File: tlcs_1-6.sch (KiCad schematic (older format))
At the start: 66 parts, among them U3 TLC5941, U4 TLC5941, U5 TLC5941, U6 TLC5941, U7 TLC5941, U8 TLC5941

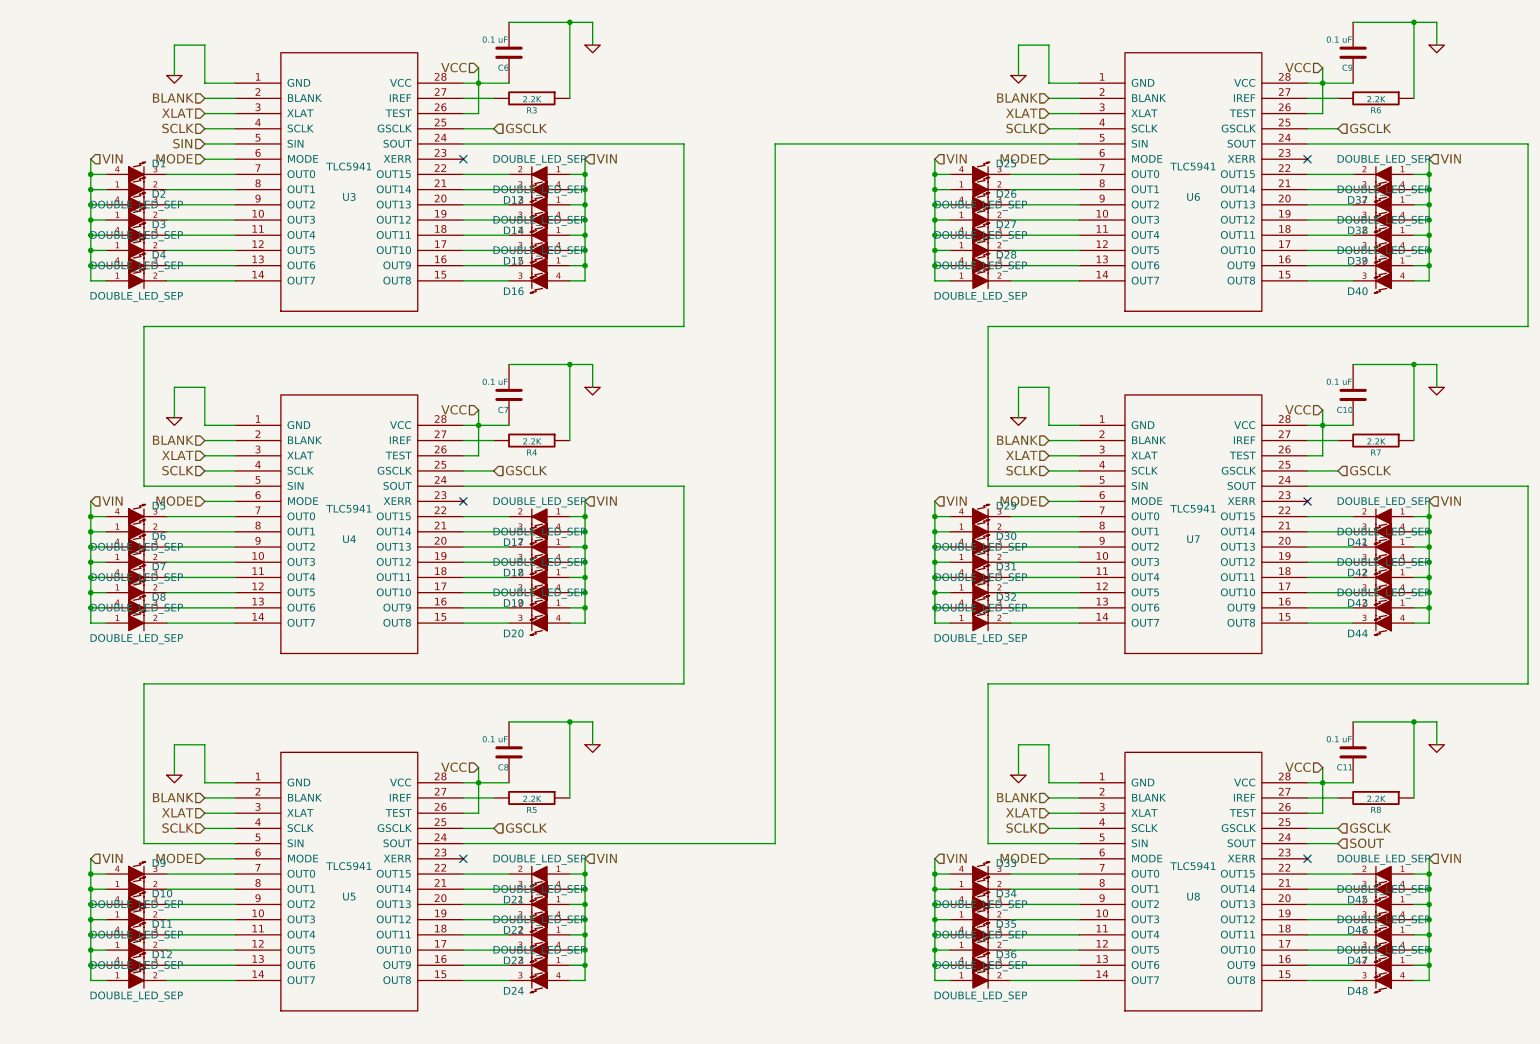
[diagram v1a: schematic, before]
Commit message: partially changed LEDs
done new footprint, added to new tca_footprints.pretty library. partially changed LEDs in schematic.
committing to go back and double check previous LED order to maintain firmware compatibility.
added /rescue-backup/ to git ignore (dont need with version control)
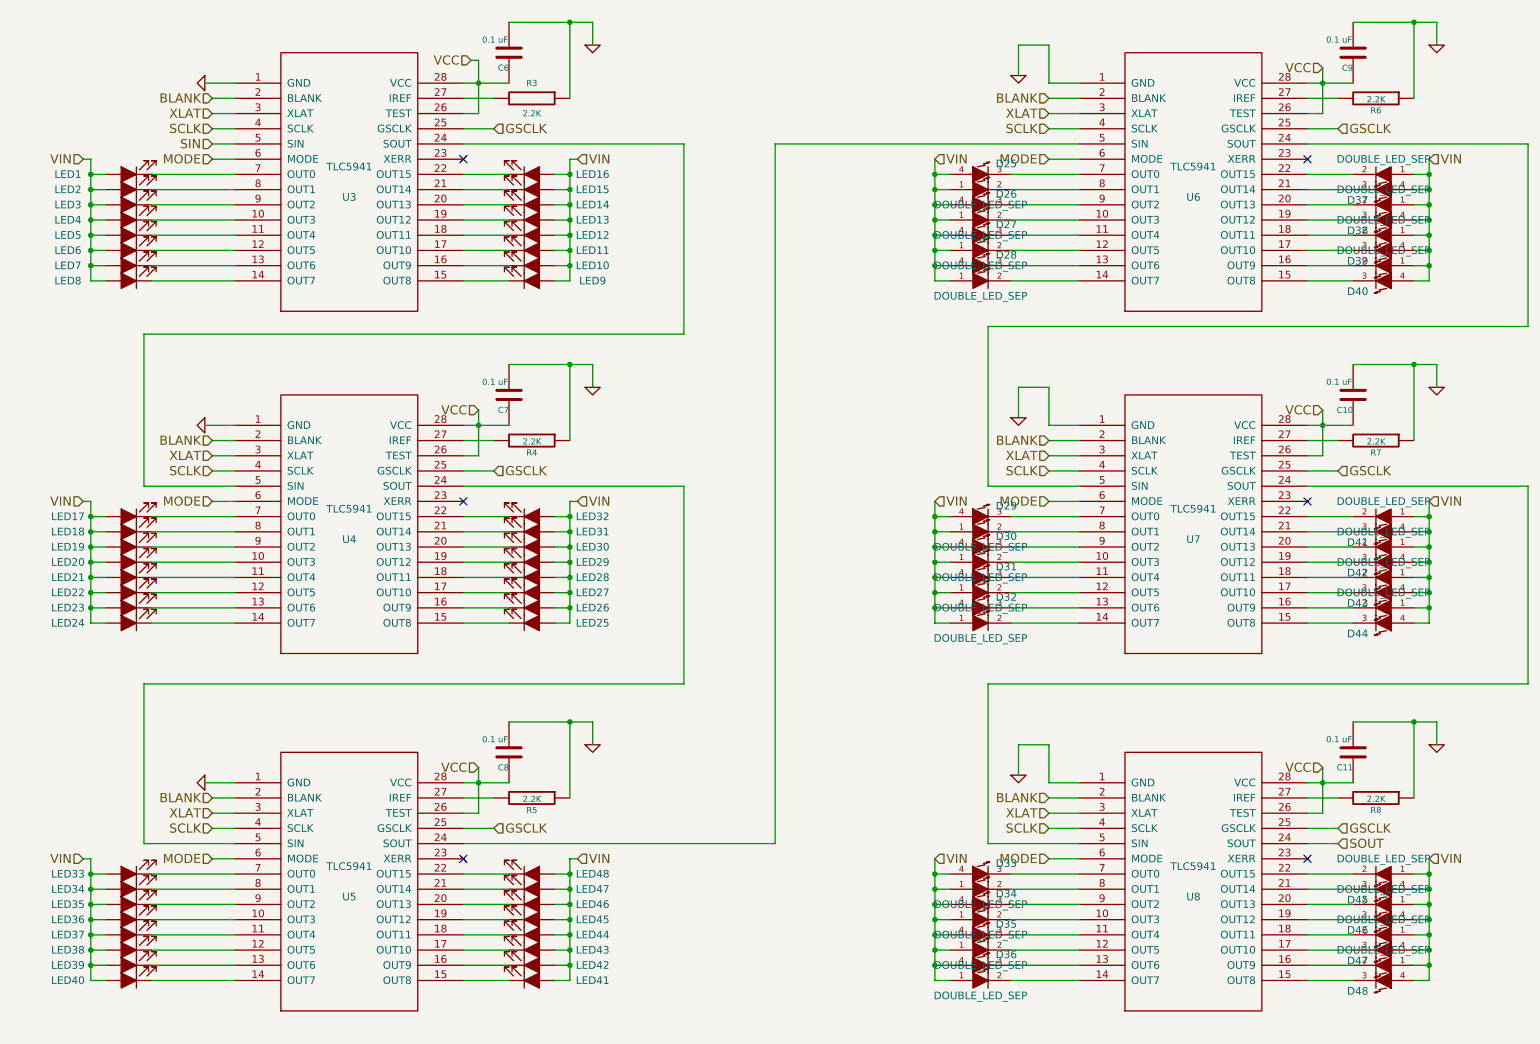
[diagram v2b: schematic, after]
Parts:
- removed D1, D10, D11, D12, D13, D14, D15, D16, D17, D18, D19, D2, D20, D21, D22, D23, D24, D3, D4, D5, D6, D7, D8, D9: DOUBLE_LED_SEP, SMD_0805_4PIN, symbol tca-rescue:DOUBLE_LED_SEP
- added LED1, LED10, LED11, LED12, LED13, LED14, LED15, LED16, LED17, LED18, LED19, LED2, LED20, LED21, LED22, LED23, LED24, LED25, LED26, LED27, LED28, LED29, LED3, LED30, LED31, LED32, LED33, LED34, LED35, LED36, LED37, LED38, LED39, LED4, LED40, LED41, LED42, LED43, LED44, LED45, LED46, LED47, LED48, LED5, LED6, LED7, LED8, LED9: LED_ALT, tca_footprints:VLDx1232G, symbol Device:LED_ALT
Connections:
- net VIN: now also LED1.2 (A), LED10.2 (A), LED11.2 (A), LED12.2 (A), LED13.2 (A), LED14.2 (A), LED15.2 (A), LED16.2 (A), LED17.2 (A), LED18.2 (A), LED19.2 (A), LED2.2 (A), LED20.2 (A), LED21.2 (A), LED22.2 (A), LED23.2 (A), LED24.2 (A), LED25.2 (A), LED26.2 (A), LED27.2 (A), LED28.2 (A), LED29.2 (A), LED3.2 (A), LED30.2 (A), LED31.2 (A), LED32.2 (A), LED33.2 (A), LED34.2 (A), LED35.2 (A), LED36.2 (A), LED37.2 (A), LED38.2 (A), LED39.2 (A), LED4.2 (A), LED40.2 (A), LED41.2 (A), LED42.2 (A), LED43.2 (A), LED44.2 (A), LED45.2 (A), LED46.2 (A), LED47.2 (A), LED48.2 (A), LED5.2 (A), LED6.2 (A), LED7.2 (A), LED8.2 (A), LED9.2 (A)
- net at U4.10 (OUT3): now also LED20.1 (K)
- net at U4.11 (OUT4): now also LED21.1 (K)
- net at U4.12 (OUT5): now also LED22.1 (K)
- net at U4.13 (OUT6): now also LED23.1 (K)
- net at U4.14 (OUT7): now also LED24.1 (K)
- net at U4.15 (OUT8): now also LED25.1 (K)
- net at U4.16 (OUT9): now also LED26.1 (K)
- net at U4.17 (OUT10): now also LED27.1 (K)
- net at U4.18 (OUT11): now also LED28.1 (K)
- net at U4.19 (OUT12): now also LED29.1 (K)
- net at U4.20 (OUT13): now also LED30.1 (K)
- net at U4.21 (OUT14): now also LED31.1 (K)
- net at U4.22 (OUT15): now also LED32.1 (K)
- net at U4.7 (OUT0): now also LED17.1 (K)
- net at U4.8 (OUT1): now also LED18.1 (K)
- net at U4.9 (OUT2): now also LED19.1 (K)
- net at U3.10 (OUT3): now also LED4.1 (K)
- net at U3.11 (OUT4): now also LED5.1 (K)
- net at U3.12 (OUT5): now also LED6.1 (K)
- net at U3.13 (OUT6): now also LED7.1 (K)
- net at U3.14 (OUT7): now also LED8.1 (K)
- net at U3.15 (OUT8): now also LED9.1 (K)
- net at U3.16 (OUT9): now also LED10.1 (K)
- net at U3.17 (OUT10): now also LED11.1 (K)
- net at U3.18 (OUT11): now also LED12.1 (K)
- net at U3.19 (OUT12): now also LED13.1 (K)
- net at U3.20 (OUT13): now also LED14.1 (K)
- net at U3.21 (OUT14): now also LED15.1 (K)
- net at U3.22 (OUT15): now also LED16.1 (K)
- net at U3.7 (OUT0): now also LED1.1 (K)
- net at U3.8 (OUT1): now also LED2.1 (K)
- net at U3.9 (OUT2): now also LED3.1 (K)
- net at U5.8 (OUT1): now also LED34.1 (K)
- net at U5.7 (OUT0): now also LED33.1 (K)
- net at U5.10 (OUT3): now also LED36.1 (K)
- net at U5.9 (OUT2): now also LED35.1 (K)
- net at U5.12 (OUT5): now also LED38.1 (K)
- net at U5.11 (OUT4): now also LED37.1 (K)
- net at U5.22 (OUT15): now also LED48.1 (K)
- net at U5.21 (OUT14): now also LED47.1 (K)
- net at U5.20 (OUT13): now also LED46.1 (K)
- net at U5.19 (OUT12): now also LED45.1 (K)
- net at U5.16 (OUT9): now also LED42.1 (K)
- net at U5.15 (OUT8): now also LED41.1 (K)
- net at U5.13 (OUT6): now also LED39.1 (K)
- net at U5.14 (OUT7): now also LED40.1 (K)
- net at U5.17 (OUT10): now also LED43.1 (K)
- net at U5.18 (OUT11): now also LED44.1 (K)

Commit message: finished changing all LEDs
LED1-LED96 added and referenced to match schematic, for zig-zag left-right pattern starting in bottom left of grid
arranged with VIN facing back-to-back so can have columns of VIN copper shape going vertically, to fit in with LED routing also on top
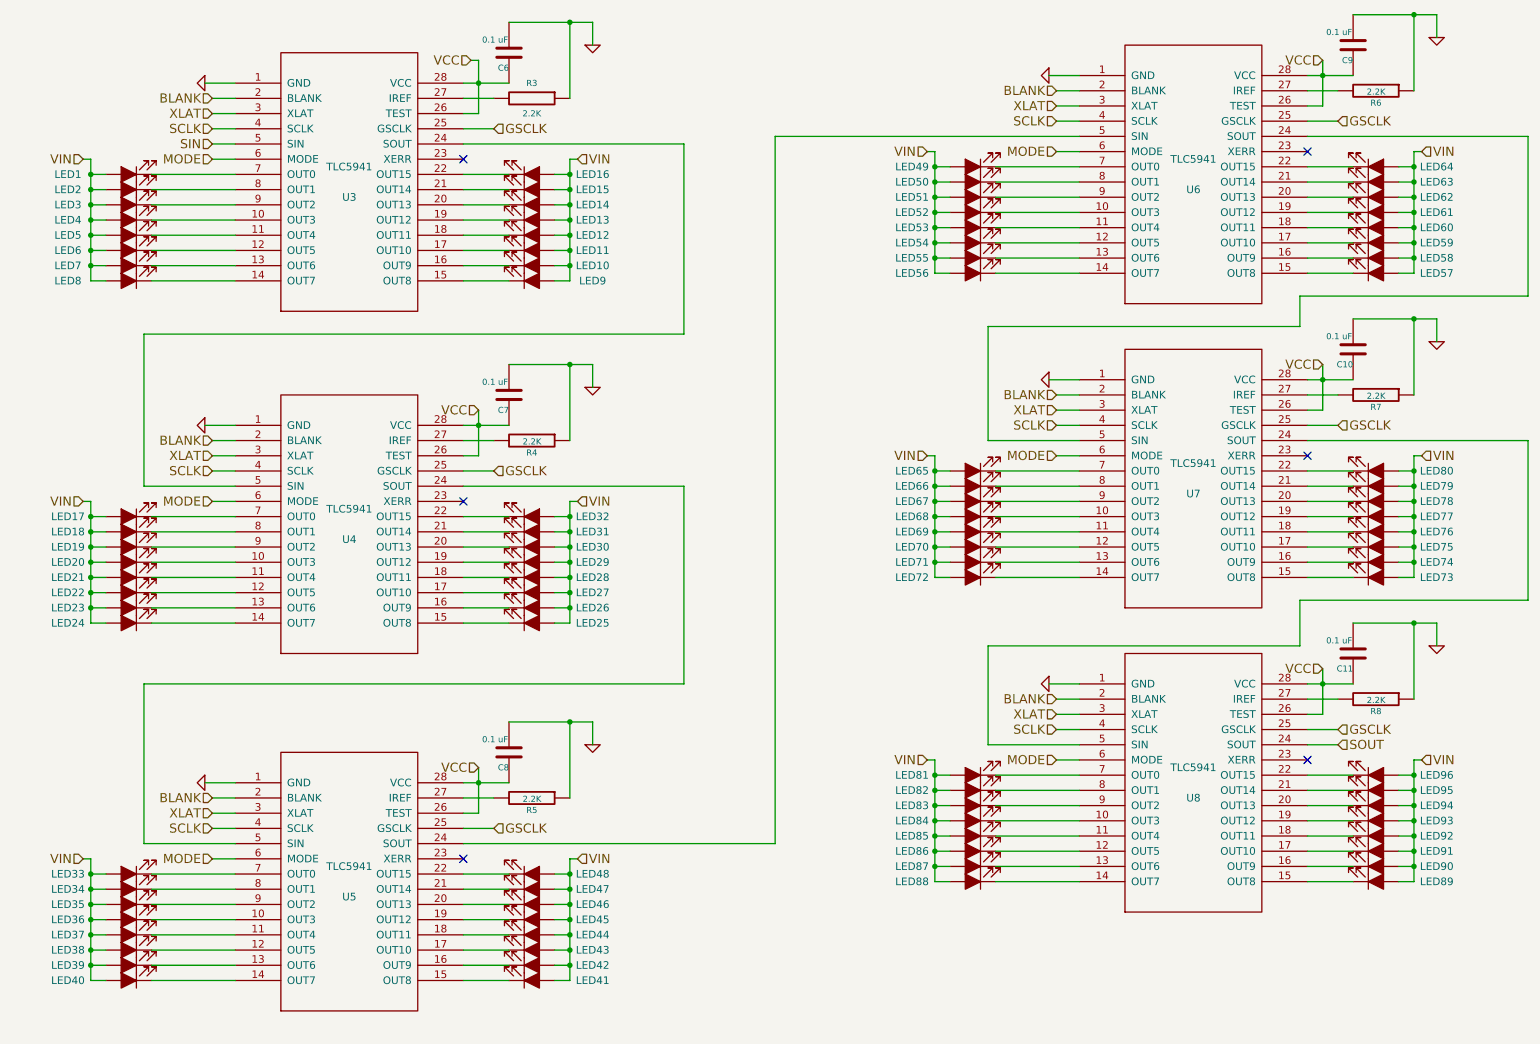
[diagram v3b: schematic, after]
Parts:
- removed D25, D26, D27, D28, D29, D30, D31, D32, D33, D34, D35, D36, D37, D38, D39, D40, D41, D42, D43, D44, D45, D46, D47, D48: DOUBLE_LED_SEP, SMD_0805_4PIN, symbol tca-rescue:DOUBLE_LED_SEP
- added LED49, LED50, LED51, LED52, LED53, LED54, LED55, LED56, LED57, LED58, LED59, LED60, LED61, LED62, LED63, LED64, LED65, LED66, LED67, LED68, LED69, LED70, LED71, LED72, LED73, LED74, LED75, LED76, LED77, LED78, LED79, LED80, LED81, LED82, LED83, LED84, LED85, LED86, LED87, LED88, LED89, LED90, LED91, LED92, LED93, LED94, LED95, LED96: LED_ALT, tca_footprints:VLDx1232G, symbol Device:LED_ALT
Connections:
- net VIN: now also LED49.2 (A), LED50.2 (A), LED51.2 (A), LED52.2 (A), LED53.2 (A), LED54.2 (A), LED55.2 (A), LED56.2 (A), LED57.2 (A), LED58.2 (A), LED59.2 (A), LED60.2 (A), LED61.2 (A), LED62.2 (A), LED63.2 (A), LED64.2 (A), LED65.2 (A), LED66.2 (A), LED67.2 (A), LED68.2 (A), LED69.2 (A), LED70.2 (A), LED71.2 (A), LED72.2 (A), LED73.2 (A), LED74.2 (A), LED75.2 (A), LED76.2 (A), LED77.2 (A), LED78.2 (A), LED79.2 (A), LED80.2 (A), LED81.2 (A), LED82.2 (A), LED83.2 (A), LED84.2 (A), LED85.2 (A), LED86.2 (A), LED87.2 (A), LED88.2 (A), LED89.2 (A), LED90.2 (A), LED91.2 (A), LED92.2 (A), LED93.2 (A), LED94.2 (A), LED95.2 (A), LED96.2 (A)
- net at U8.10 (OUT3): now also LED84.1 (K)
- net at U8.11 (OUT4): now also LED85.1 (K)
- net at U8.12 (OUT5): now also LED86.1 (K)
- net at U8.13 (OUT6): now also LED87.1 (K)
- net at U8.14 (OUT7): now also LED88.1 (K)
- net at U8.15 (OUT8): now also LED89.1 (K)
- net at U8.16 (OUT9): now also LED90.1 (K)
- net at U8.17 (OUT10): now also LED91.1 (K)
- net at U8.18 (OUT11): now also LED92.1 (K)
- net at U8.19 (OUT12): now also LED93.1 (K)
- net at U8.20 (OUT13): now also LED94.1 (K)
- net at U8.21 (OUT14): now also LED95.1 (K)
- net at U8.22 (OUT15): now also LED96.1 (K)
- net at U8.7 (OUT0): now also LED81.1 (K)
- net at U8.8 (OUT1): now also LED82.1 (K)
- net at U8.9 (OUT2): now also LED83.1 (K)
- net at U7.10 (OUT3): now also LED68.1 (K)
- net at U7.11 (OUT4): now also LED69.1 (K)
- net at U7.12 (OUT5): now also LED70.1 (K)
- net at U7.13 (OUT6): now also LED71.1 (K)
- net at U7.14 (OUT7): now also LED72.1 (K)
- net at U7.15 (OUT8): now also LED73.1 (K)
- net at U7.16 (OUT9): now also LED74.1 (K)
- net at U7.17 (OUT10): now also LED75.1 (K)
- net at U7.18 (OUT11): now also LED76.1 (K)
- net at U7.19 (OUT12): now also LED77.1 (K)
- net at U7.20 (OUT13): now also LED78.1 (K)
- net at U7.21 (OUT14): now also LED79.1 (K)
- net at U7.22 (OUT15): now also LED80.1 (K)
- net at U7.7 (OUT0): now also LED65.1 (K)
- net at U7.8 (OUT1): now also LED66.1 (K)
- net at U7.9 (OUT2): now also LED67.1 (K)
- net at U6.10 (OUT3): now also LED52.1 (K)
- net at U6.11 (OUT4): now also LED53.1 (K)
- net at U6.12 (OUT5): now also LED54.1 (K)
- net at U6.13 (OUT6): now also LED55.1 (K)
- net at U6.14 (OUT7): now also LED56.1 (K)
- net at U6.15 (OUT8): now also LED57.1 (K)
- net at U6.16 (OUT9): now also LED58.1 (K)
- net at U6.17 (OUT10): now also LED59.1 (K)
- net at U6.18 (OUT11): now also LED60.1 (K)
- net at U6.19 (OUT12): now also LED61.1 (K)
- net at U6.20 (OUT13): now also LED62.1 (K)
- net at U6.21 (OUT14): now also LED63.1 (K)
- net at U6.22 (OUT15): now also LED64.1 (K)
- net at U6.7 (OUT0): now also LED49.1 (K)
- net at U6.8 (OUT1): now also LED50.1 (K)
- net at U6.9 (OUT2): now also LED51.1 (K)
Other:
- moved on the sheet: C10, C11, C9, R6, R7, R8, U6, U7, U8

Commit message: design rules & annotation text
adjusted design rules: 0.25/0.2mm track/gap (larger for power nets), via 0.9/0.5mm (smaller 0.6/0.25mm for thermal vias), 0.05mm solder mask clearance
replaced all vias with 0.9/0.5mm by default, this and design rules should solve most of DRC issues
added some common track widths
placed driver chips and routed some important nets & surrounding passives first
neatened placement on schematic page and added heading text for each are
deleted duplicate Edge.cuts line on right side of board which was causing DRC, not sure whether I introduced or existing
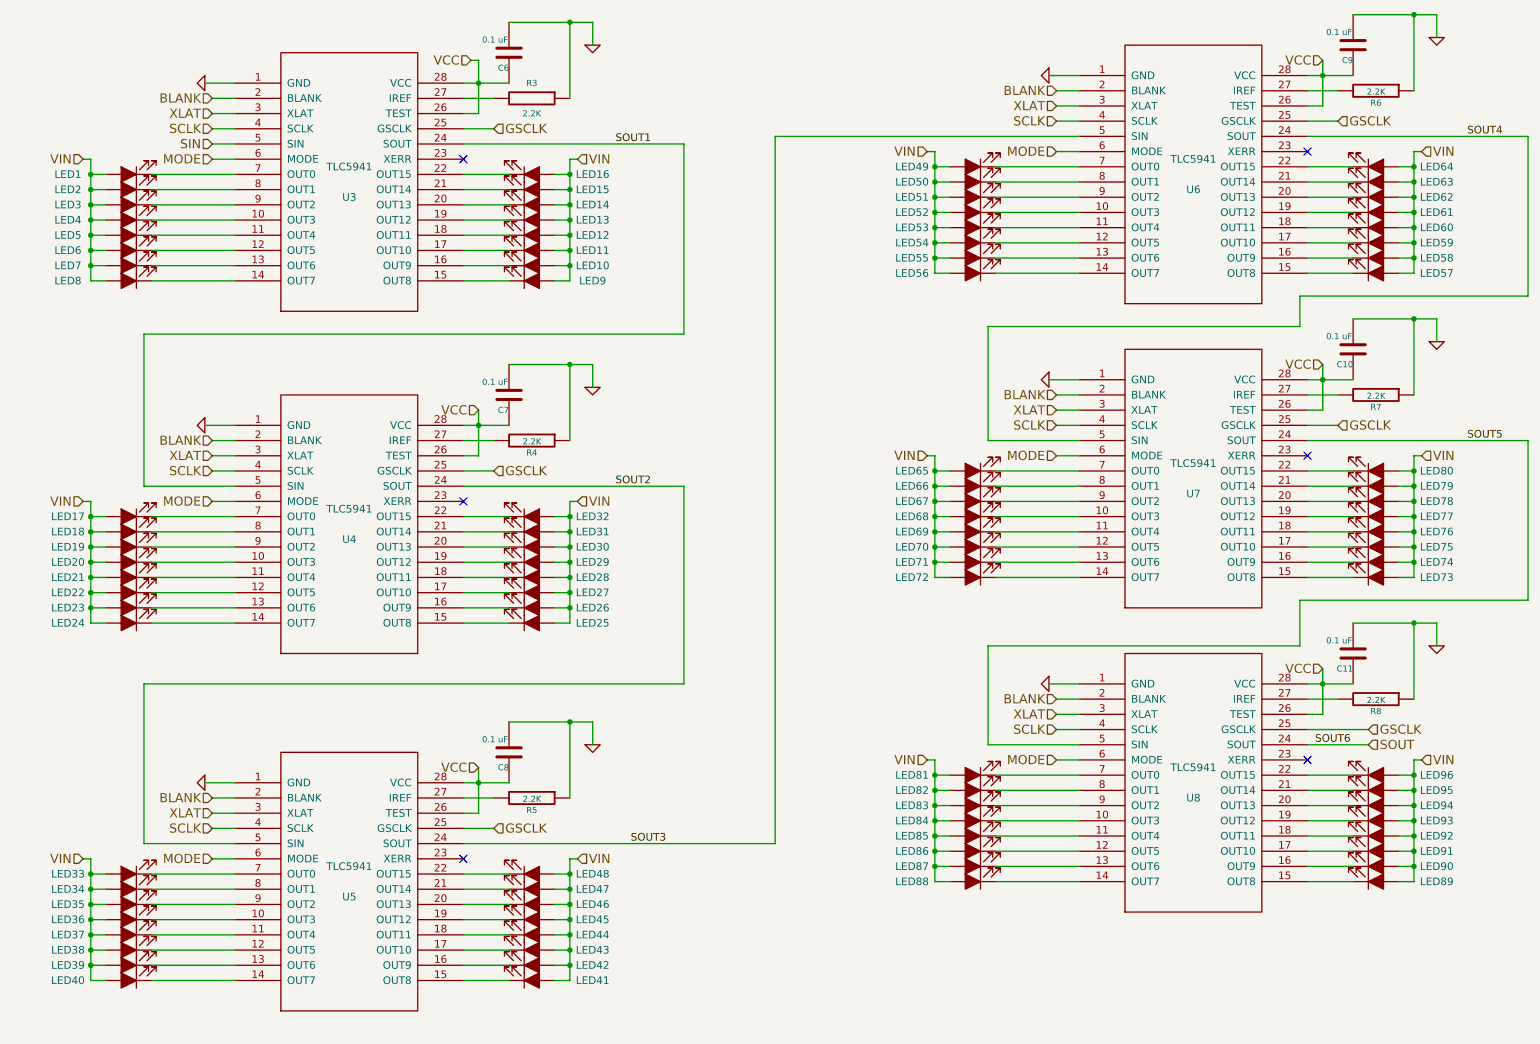
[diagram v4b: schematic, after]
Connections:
- net SOUT2: now reaches U4.24 (SOUT), U5.5 (SIN)
- net SOUT1: now reaches U3.24 (SOUT), U4.5 (SIN)
- net SOUT5: now reaches U7.24 (SOUT), U8.5 (SIN)
- net SOUT4: now reaches U6.24 (SOUT), U7.5 (SIN)
- net SOUT3: now reaches U5.24 (SOUT), U6.5 (SIN)
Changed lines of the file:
@@
 	10000 5050 10000 4550
 Wire Wire Line
-	9300 5250 9500 5250
+	9300 5250 9700 5250
 Connection ~ 10000 4550
 Wire Wire Line
@@
 Text HLabel 9500 1250 2    60   Input ~ 0
 GSCLK
-Text HLabel 9500 5250 2    60   Input ~ 0
+Text HLabel 9700 5250 2    60   Input ~ 0
 GSCLK
 Text HLabel 9400 4850 0    60   Input ~ 0
@@
 Text HLabel 9400 850  0    60   Input ~ 0
 VCC
-Text HLabel 9500 5350 2    60   Input ~ 0
+Text HLabel 9700 5350 2    60   Input ~ 0
 SOUT
-Wire Wire Line
-	9300 5350 9500 5350
 Wire Wire Line
 	4450 2200 4450 2300
@@
 	-1   0    0    1
 $EndComp
+Text Label 4750 1400 0    50   ~ 0
+SOUT1
+Text Label 4750 3650 0    50   ~ 0
+SOUT2
+Text Label 4850 6000 0    50   ~ 0
+SOUT3
+Text Label 10350 1350 0    50   ~ 0
+SOUT4
+Text Label 10350 3350 0    50   ~ 0
+SOUT5
+Text Label 9350 5350 0    50   ~ 0
+SOUT6
+Wire Wire Line
+	9300 5350 9700 5350
 $EndSCHEMATC
